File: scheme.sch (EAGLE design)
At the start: 34 parts, among them J1 22-05-7048-04, J2 22-05-7028-02

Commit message: Minor fix of routes
Signed-off-by: Nikita 'webconn' Maslov <wkernelteam@gmail.com>
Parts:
- R10, R9: device rcl:R-EU_R1206 -> resistor:R-EU_R0805
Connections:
- net PB5: now also R10.1; no longer R9.2
- net VCC: now also R9.2; no longer R10.1
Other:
- moved on the sheet: R10, R9
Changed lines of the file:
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@@
 <part name="P+17" library="supply1" deviceset="+12V" device=""/>
 <part name="P+19" library="supply1" deviceset="VCC" device=""/>
-<part name="R9" library="rcl" deviceset="R-EU_" device="R1206" value="0"/>
-<part name="R10" library="rcl" deviceset="R-EU_" device="R1206" value="0"/>
 <part name="P+18" library="supply1" deviceset="VCC" device=""/>
 <part name="J2" library="con-molex" deviceset="22-?-02" device="05-7028"/>
+<part name="R9" library="resistor" deviceset="R-EU_" device="R0805" value="0"/>
+<part name="R10" library="resistor" deviceset="R-EU_" device="R0805" value="0"/>
 </parts>
 <sheets>
@@
 <instance part="P+17" gate="1" x="68.58" y="45.72" rot="R180"/>
 <instance part="P+19" gate="VCC" x="83.82" y="71.12"/>
-<instance part="R9" gate="G$1" x="139.7" y="71.12"/>
-<instance part="R10" gate="G$1" x="124.46" y="71.12"/>
 <instance part="P+18" gate="VCC" x="116.84" y="76.2"/>
 <instance part="J2" gate="-1" x="63.5" y="55.88" rot="R180"/>
 <instance part="J2" gate="-2" x="63.5" y="58.42" rot="R180"/>
+<instance part="R9" gate="G$1" x="124.46" y="71.12" rot="R180"/>
+<instance part="R10" gate="G$1" x="139.7" y="71.12" rot="R180"/>
 </instances>
 <busses>
@@
 </segment>
 <segment>
-<pinref part="R10" gate="G$1" pin="1"/>
 <wire x1="119.38" y1="71.12" x2="116.84" y2="71.12" width="0.1524" layer="91"/>
 <wire x1="116.84" y1="71.12" x2="116.84" y2="73.66" width="0.1524" layer="91"/>
 <pinref part="P+18" gate="VCC" pin="VCC"/>
+<pinref part="R9" gate="G$1" pin="2"/>
 </segment>
 </net>
@@
 </segment>
 <segment>
-<pinref part="R9" gate="G$1" pin="2"/>
 <wire x1="144.78" y1="71.12" x2="154.94" y2="71.12" width="0.1524" layer="91"/>
 <label x="149.86" y="71.12" size="1.778" layer="95"/>
+<pinref part="R10" gate="G$1" pin="1"/>
 </segment>
 </net>
@@
 <wire x1="111.76" y1="66.04" x2="132.08" y2="66.04" width="0.1524" layer="91"/>
 <wire x1="132.08" y1="66.04" x2="132.08" y2="71.12" width="0.1524" layer="91"/>
-<pinref part="R9" gate="G$1" pin="1"/>
 <wire x1="132.08" y1="71.12" x2="134.62" y2="71.12" width="0.1524" layer="91"/>
-<pinref part="R10" gate="G$1" pin="2"/>
 <wire x1="129.54" y1="71.12" x2="132.08" y2="71.12" width="0.1524" layer="91"/>
 <junction x="132.08" y="71.12"/>
-</segment>
-</net>
+<pinref part="R9" gate="G$1" pin="1"/>
+<pinref part="R10" gate="G$1" pin="2"/>
+</segment>
+</net>

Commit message: Add BOOT button and fix isolation
Signed-off-by: Nikita 'webconn' Maslov <wkernelteam@gmail.com>
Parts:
- removed LED1: (no value), SparkFun-LED:LED5MM
- added R11, R12: 0, rcl:R-EU_R1206
- added S2: (no value), switch-omron:31-XX
- R4: value 300 -> 10K
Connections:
- net RXLED renamed LED
- removed net N$12: LED1.A, R4.1
- removed net TXLED: LED1.C, U$1.(XCK1/CTS)PD5
- new net HWB: R4.1, S2.S, U$1.(HWB)PE2
- net +5V: now also U$4.+VOUT; no longer U$3.+VOUT
- net GND: now also R11.1, R11.2, R12.1, R12.2, S2.P
- net RELAY: now also U$1.(XCK1/CTS)PD5; no longer U$1.(HWB)PE2
- net VCC: now also U$3.+VOUT; no longer U$4.+VOUT
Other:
- moved on the sheet: R4, U$3, U$4

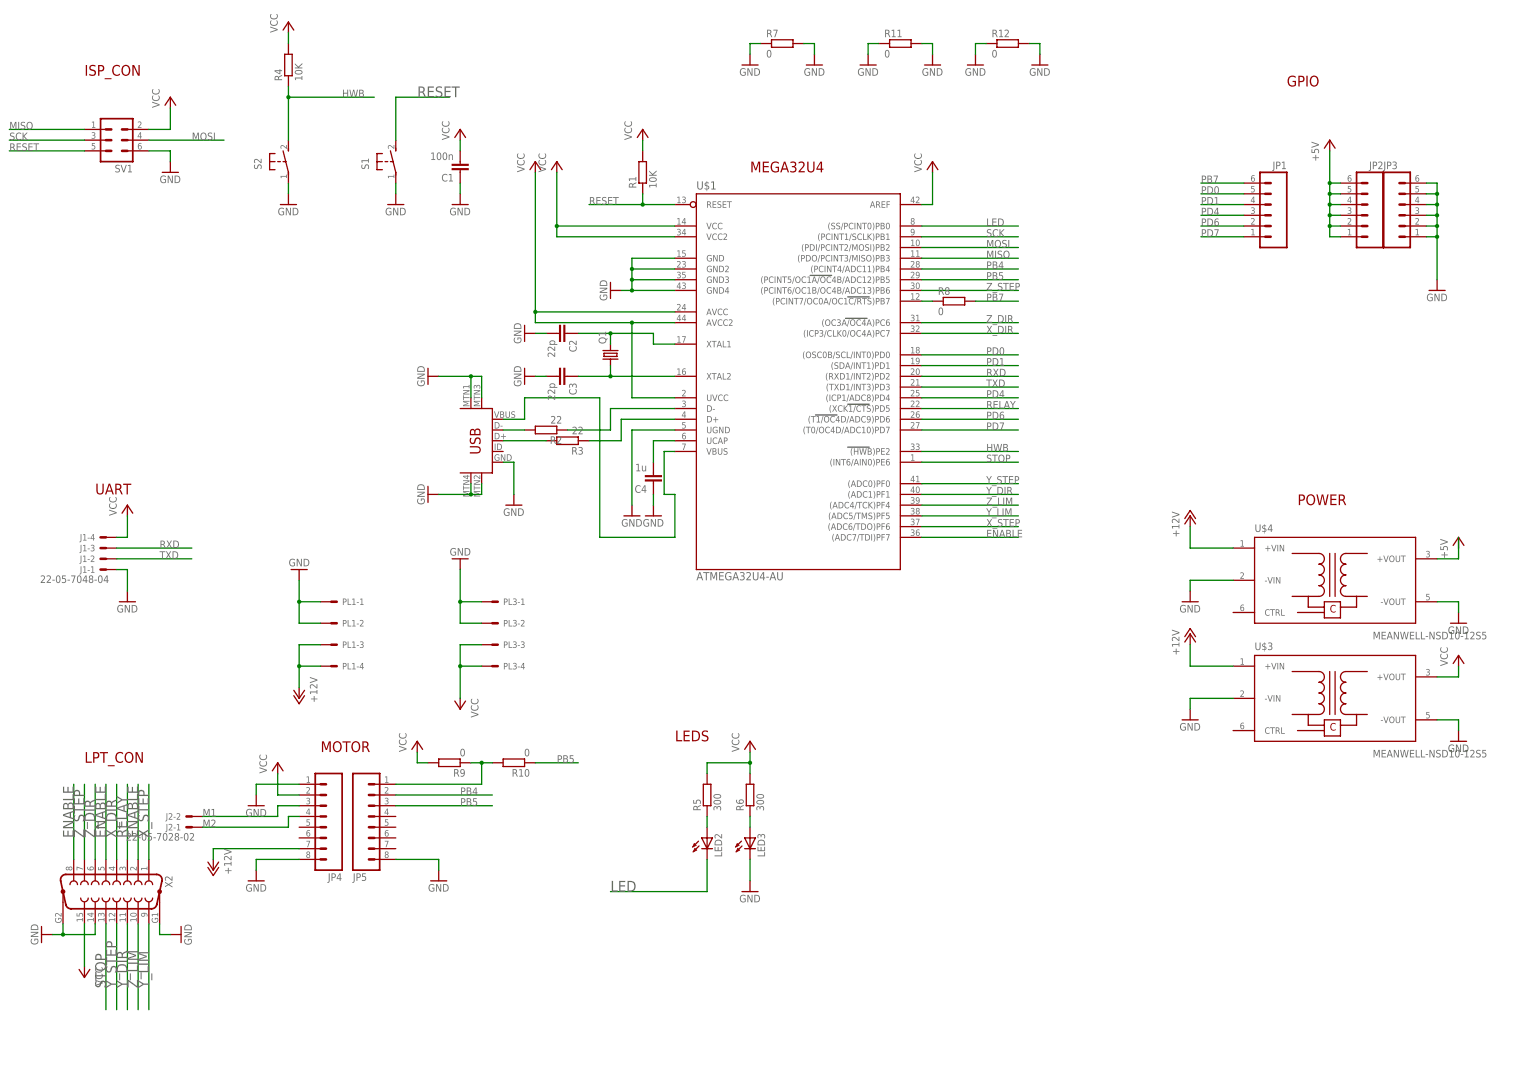
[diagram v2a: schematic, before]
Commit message: Add extra capacitors and rework silk
Signed-off-by: Nikita 'webconn' Maslov <wkernelteam@gmail.com>
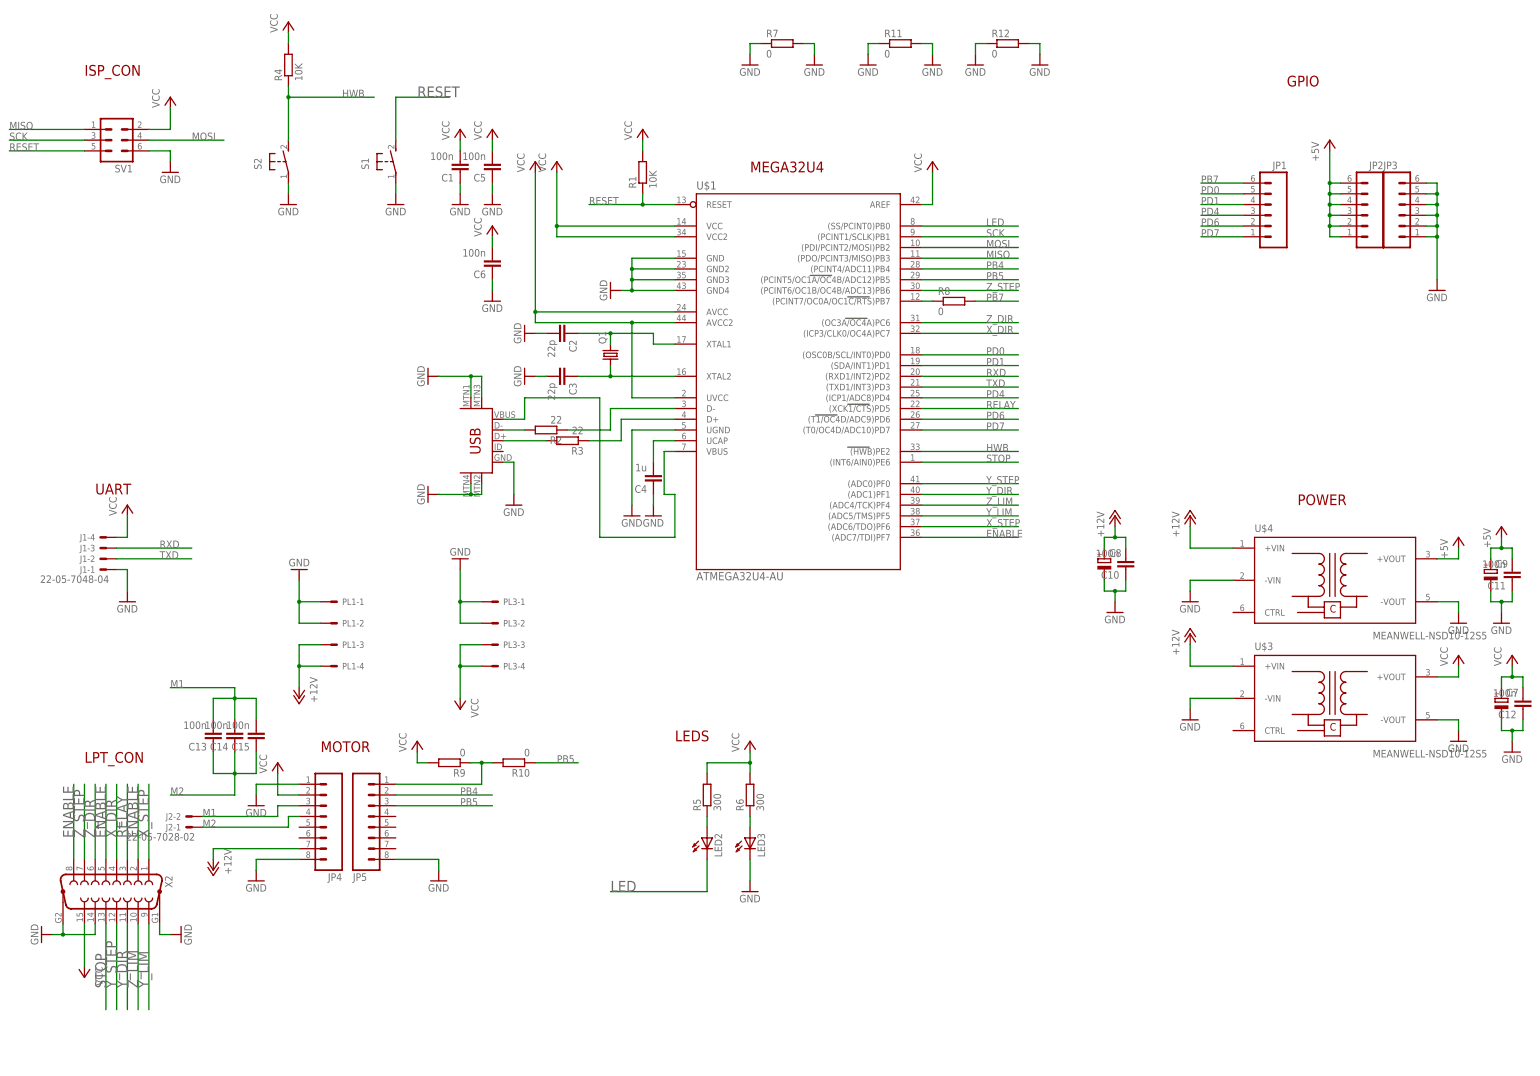
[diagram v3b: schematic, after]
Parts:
- added C10, C11, C12, C13, C14, C15, C5, C6: 100n, resistor:C-EUC0805
- added C7, C8, C9: (no value), rcl:CPOL-EUE2.5-6
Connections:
- net +12V: now also C10.2, C8.+
- net +5V: now also C11.2, C9.+
- net GND: now also C10.1, C11.1, C12.1, C5.1, C6.1, C7.-, C8.-, C9.-
- net M1: now also C13.2, C14.2, C15.2
- net M2: now also C13.1, C14.1, C15.1
- net VCC: now also C12.2, C5.2, C6.2, C7.+
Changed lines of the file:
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@@
 <part name="GND31" library="supply1" deviceset="GND" device=""/>
 <part name="GND32" library="supply1" deviceset="GND" device=""/>
+<part name="C5" library="resistor" deviceset="C-EU" device="C0805" value="100n"/>
+<part name="P+21" library="supply1" deviceset="VCC" device=""/>
+<part name="GND33" library="supply1" deviceset="GND" device=""/>
+<part name="C6" library="resistor" deviceset="C-EU" device="C0805" value="100n"/>
+<part name="P+22" library="supply1" deviceset="VCC" device=""/>
+<part name="GND34" library="supply1" deviceset="GND" device=""/>
+<part name="C8" library="rcl" deviceset="CPOL-EU" device="E2.5-6"/>
+<part name="C9" library="rcl" deviceset="CPOL-EU" device="E2.5-6"/>
+<part name="P+23" library="supply1" deviceset="+12V" device=""/>
+<part name="GND35" library="supply1" deviceset="GND" device=""/>
+<part name="P+24" library="supply1" deviceset="+5V" device=""/>
+<part name="GND36" library="supply1" deviceset="GND" device=""/>
+<part name="C7" library="rcl" deviceset="CPOL-EU" device="E2.5-6"/>
+<part name="P+25" library="supply1" deviceset="VCC" device=""/>
+<part name="GND37" library="supply1" deviceset="GND" device=""/>
+<part name="C10" library="resistor" deviceset="C-EU" device="C0805" value="100n"/>
+<part name="C11" library="resistor" deviceset="C-EU" device="C0805" value="100n"/>
+<part name="C12" library="resistor" deviceset="C-EU" device="C0805" value="100n"/>
+<part name="C13" library="resistor" deviceset="C-EU" device="C0805" value="100n"/>
+<part name="C14" library="resistor" deviceset="C-EU" device="C0805" value="100n"/>
+<part name="C15" library="resistor" deviceset="C-EU" device="C0805" value="100n"/>
 </parts>
 <sheets>
@@
 <instance part="GND31" gate="1" x="248.92" y="236.22"/>
 <instance part="GND32" gate="1" x="264.16" y="236.22"/>
+<instance part="C5" gate="G$1" x="134.62" y="210.82" rot="R180"/>
+<instance part="P+21" gate="VCC" x="134.62" y="220.98"/>
+<instance part="GND33" gate="1" x="134.62" y="203.2"/>
+<instance part="C6" gate="G$1" x="134.62" y="187.96" rot="R180"/>
+<instance part="P+22" gate="VCC" x="134.62" y="198.12"/>
+<instance part="GND34" gate="1" x="134.62" y="180.34"/>
+<instance part="C8" gate="G$1" x="279.4" y="119.38"/>
+<instance part="C9" gate="G$1" x="370.84" y="116.84"/>
+<instance part="P+23" gate="1" x="281.94" y="129.54"/>
+<instance part="GND35" gate="1" x="281.94" y="106.68"/>
+<instance part="P+24" gate="1" x="373.38" y="127"/>
+<instance part="GND36" gate="1" x="373.38" y="104.14"/>
+<instance part="C7" gate="G$1" x="373.38" y="86.36"/>
+<instance part="P+25" gate="VCC" x="375.92" y="96.52"/>
+<instance part="GND37" gate="1" x="375.92" y="73.66"/>
+<instance part="C10" gate="G$1" x="284.48" y="116.84" rot="R180"/>
+<instance part="C11" gate="G$1" x="375.92" y="114.3" rot="R180"/>
+<instance part="C12" gate="G$1" x="378.46" y="83.82" rot="R180"/>
+<instance part="C13" gate="G$1" x="68.58" y="76.2" rot="R180"/>
+<instance part="C14" gate="G$1" x="73.66" y="76.2" rot="R180"/>
+<instance part="C15" gate="G$1" x="78.74" y="76.2" rot="R180"/>
 </instances>
 <busses>
@@
 <wire x1="264.16" y1="241.3" x2="264.16" y2="238.76" width="0.1524" layer="91"/>
 </segment>
+<segment>
+<pinref part="C5" gate="G$1" pin="1"/>
+<pinref part="GND33" gate="1" pin="GND"/>
+<wire x1="134.62" y1="208.28" x2="134.62" y2="205.74" width="0.1524" layer="91"/>
+</segment>
+<segment>
+<pinref part="C6" gate="G$1" pin="1"/>
+<pinref part="GND34" gate="1" pin="GND"/>
+<wire x1="134.62" y1="185.42" x2="134.62" y2="182.88" width="0.1524" layer="91"/>
+</segment>
+<segment>
+<pinref part="C8" gate="G$1" pin="-"/>
+<wire x1="279.4" y1="114.3" x2="279.4" y2="111.76" width="0.1524" layer="91"/>
+<wire x1="279.4" y1="111.76" x2="281.94" y2="111.76" width="0.1524" layer="91"/>
+<pinref part="GND35" gate="1" pin="GND"/>
+<wire x1="281.94" y1="111.76" x2="281.94" y2="109.22" width="0.1524" layer="91"/>
+<pinref part="C10" gate="G$1" pin="1"/>
+<wire x1="281.94" y1="111.76" x2="284.48" y2="111.76" width="0.1524" layer="91"/>
+<wire x1="284.48" y1="111.76" x2="284.48" y2="114.3" width="0.1524" layer="91"/>
+<junction x="281.94" y="111.76"/>
+</segment>
+<segment>
+<pinref part="C9" gate="G$1" pin="-"/>
+<wire x1="370.84" y1="111.76" x2="370.84" y2="109.22" width="0.1524" layer="91"/>
+<wire x1="370.84" y1="109.22" x2="373.38" y2="109.22" width="0.1524" layer="91"/>
+<pinref part="GND36" gate="1" pin="GND"/>
+<wire x1="373.38" y1="109.22" x2="373.38" y2="106.68" width="0.1524" layer="91"/>
+<pinref part="C11" gate="G$1" pin="1"/>
+<wire x1="373.38" y1="109.22" x2="375.92" y2="109.22" width="0.1524" layer="91"/>
+<wire x1="375.92" y1="109.22" x2="375.92" y2="111.76" width="0.1524" layer="91"/>
+<junction x="373.38" y="109.22"/>
+</segment>
+<segment>
+<pinref part="C7" gate="G$1" pin="-"/>
+<wire x1="373.38" y1="81.28" x2="373.38" y2="78.74" width="0.1524" layer="91"/>
+<pinref part="C12" gate="G$1" pin="1"/>
+<wire x1="373.38" y1="78.74" x2="375.92" y2="78.74" width="0.1524" layer="91"/>
+<wire x1="375.92" y1="78.74" x2="378.46" y2="78.74" width="0.1524" layer="91"/>
+<wire x1="378.46" y1="78.74" x2="378.46" y2="81.28" width="0.1524" layer="91"/>
+<pinref part="GND37" gate="1" pin="GND"/>
+<wire x1="375.92" y1="78.74" x2="375.92" y2="76.2" width="0.1524" layer="91"/>
+<junction x="375.92" y="78.74"/>
+</segment>
 </net>
 <net name="RESET" class="0">
@@
 <wire x1="86.36" y1="243.84" x2="86.36" y2="241.3" width="0.1524" layer="91"/>
 </segment>
+<segment>
+<pinref part="P+21" gate="VCC" pin="VCC"/>
+<pinref part="C5" gate="G$1" pin="2"/>
+<wire x1="134.62" y1="218.44" x2="134.62" y2="215.9" width="0.1524" layer="91"/>
+</segment>
+<segment>
+<pinref part="P+22" gate="VCC" pin="VCC"/>
+<pinref part="C6" gate="G$1" pin="2"/>
+<wire x1="134.62" y1="195.58" x2="134.62" y2="193.04" width="0.1524" layer="91"/>
+</segment>
+<segment>
+<pinref part="C7" gate="G$1" pin="+"/>
+<wire x1="373.38" y1="88.9" x2="373.38" y2="91.44" width="0.1524" layer="91"/>
+<pinref part="C12" gate="G$1" pin="2"/>
+<wire x1="373.38" y1="91.44" x2="375.92" y2="91.44" width="0.1524" layer="91"/>
+<wire x1="375.92" y1="91.44" x2="378.46" y2="91.44" width="0.1524" layer="91"/>
+<wire x1="378.46" y1="91.44" x2="378.46" y2="88.9" width="0.1524" layer="91"/>
+<pinref part="P+25" gate="VCC" pin="VCC"/>
+<wire x1="375.92" y1="91.44" x2="375.92" y2="93.98" width="0.1524" layer="91"/>
+<junction x="375.92" y="91.44"/>
+</segment>
 </net>
 <net name="N$4" class="0">
@@
 <wire x1="68.58" y1="50.8" x2="68.58" y2="48.26" width="0.1524" layer="91"/>
 <pinref part="P+17" gate="1" pin="+12V"/>
+</segment>
+<segment>
+<pinref part="C8" gate="G$1" pin="+"/>
+<wire x1="279.4" y1="121.92" x2="279.4" y2="124.46" width="0.1524" layer="91"/>
+<wire x1="279.4" y1="124.46" x2="281.94" y2="124.46" width="0.1524" layer="91"/>
+<pinref part="P+23" gate="1" pin="+12V"/>
+<wire x1="281.94" y1="127" x2="281.94" y2="124.46" width="0.1524" layer="91"/>
+<pinref part="C10" gate="G$1" pin="2"/>
+<wire x1="281.94" y1="124.46" x2="284.48" y2="124.46" width="0.1524" layer="91"/>
+<wire x1="284.48" y1="124.46" x2="284.48" y2="121.92" width="0.1524" layer="91"/>
+<junction x="281.94" y="124.46"/>
 </segment>
 </net>
@@
 <wire x1="358.14" y1="119.38" x2="363.22" y2="119.38" width="0.1524" layer="91"/>
 <wire x1="363.22" y1="119.38" x2="363.22" y2="121.92" width="0.1524" layer="91"/>
-<wire x1="363.22" y1="121.92" x2="363.22" y2="124.46" width="0.1524" layer="91"/>
 <pinref part="U$4" gate="G$1" pin="+VOUT"/>
+</segment>
+<segment>
+<pinref part="C9" gate="G$1" pin="+"/>
+<wire x1="370.84" y1="119.38" x2="370.84" y2="121.92" width="0.1524" layer="91"/>
+<wire x1="370.84" y1="121.92" x2="373.38" y2="121.92" width="0.1524" layer="91"/>
+<pinref part="P+24" gate="1" pin="+5V"/>
+<wire x1="373.38" y1="121.92" x2="373.38" y2="124.46" width="0.1524" layer="91"/>
+<pinref part="C11" gate="G$1" pin="2"/>
+<wire x1="373.38" y1="121.92" x2="375.92" y2="121.92" width="0.1524" layer="91"/>
+<wire x1="375.92" y1="121.92" x2="375.92" y2="119.38" width="0.1524" layer="91"/>
+<junction x="373.38" y="121.92"/>
 </segment>
 </net>
@@
 <pinref part="J2" gate="-2" pin="S"/>
 </segment>
+<segment>
+<pinref part="C13" gate="G$1" pin="2"/>
+<wire x1="68.58" y1="81.28" x2="68.58" y2="86.36" width="0.1524" layer="91"/>
+<pinref part="C14" gate="G$1" pin="2"/>
+<wire x1="73.66" y1="81.28" x2="73.66" y2="86.36" width="0.1524" layer="91"/>
+<wire x1="68.58" y1="86.36" x2="73.66" y2="86.36" width="0.1524" layer="91"/>
+<pinref part="C15" gate="G$1" pin="2"/>
+<wire x1="78.74" y1="81.28" x2="78.74" y2="86.36" width="0.1524" layer="91"/>
+<wire x1="73.66" y1="86.36" x2="78.74" y2="86.36" width="0.1524" layer="91"/>
+<junction x="73.66" y="86.36"/>
+<wire x1="73.66" y1="86.36" x2="73.66" y2="88.9" width="0.1524" layer="91"/>
+<wire x1="73.66" y1="88.9" x2="58.42" y2="88.9" width="0.1524" layer="91"/>
+<label x="58.42" y="88.9" size="1.778" layer="95"/>
+</segment>
 </net>
 <net name="M2" class="0">
@@
 <pinref part="J2" gate="-1" pin="S"/>
 </segment>
-</net>
+<segment>
+<pinref part="C13" gate="G$1" pin="1"/>
+<wire x1="68.58" y1="73.66" x2="68.58" y2="68.58" width="0.1524" layer="91"/>
+<pinref part="C14" gate="G$1" pin="1"/>
+<wire x1="73.66" y1="73.66" x2="73.66" y2="68.58" width="0.1524" layer="91"/>
+<pinref part="C15" gate="G$1" pin="1"/>
+<wire x1="78.74" y1="73.66" x2="78.74" y2="68.58" width="0.1524" layer="91"/>
+<wire x1="73.66" y1="68.58" x2="78.74" y2="68.58" width="0.1524" layer="91"/>
+<wire x1="68.58" y1="68.58" x2="73.66" y2="68.58" width="0.1524" layer="91"/>
+<junction x="73.66" y="68.58"/>
+<wire x1="73.66" y1="68.58" x2="73.66" y2="63.5" width="0.1524" layer="91"/>
+<wire x1="73.66" y1="63.5" x2="58.42" y2="63.5" width="0.1524" layer="91"/>
+<label x="58.42" y="63.5" size="1.778" layer="95"/>
+</segment>
+</net>

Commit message: Add USB power jumper
Signed-off-by: Nikita 'webconn' Maslov <wkernelteam@gmail.com>
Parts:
- added JP6: M02PTH, SparkFun-Connectors:M02PTH
- added R13: 0, rcl:R-EU_R1206
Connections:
- new net N$12: JP6.1, R13.1
- net N$11: now also R13.2
- net VCC: now also JP6.2
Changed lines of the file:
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@@
 <part name="C14" library="resistor" deviceset="C-EU" device="C0805" value="100n"/>
 <part name="C15" library="resistor" deviceset="C-EU" device="C0805" value="100n"/>
+<part name="JP6" library="SparkFun-Connectors" deviceset="M02" device="PTH"/>
+<part name="P+26" library="supply1" deviceset="VCC" device=""/>
+<part name="R13" library="rcl" deviceset="R-EU_" device="R1206" value="0"/>
 </parts>
 <sheets>
@@
 <instance part="C14" gate="G$1" x="73.66" y="76.2" rot="R180"/>
 <instance part="C15" gate="G$1" x="78.74" y="76.2" rot="R180"/>
+<instance part="JP6" gate="G$1" x="175.26" y="116.84" rot="R180"/>
+<instance part="P+26" gate="VCC" x="157.48" y="114.3" rot="R90"/>
+<instance part="R13" gate="G$1" x="154.94" y="124.46" rot="R90"/>
 </instances>
 <busses>
@@
 <junction x="375.92" y="91.44"/>
 </segment>
+<segment>
+<pinref part="P+26" gate="VCC" pin="VCC"/>
+<pinref part="JP6" gate="G$1" pin="2"/>
+<wire x1="160.02" y1="114.3" x2="167.64" y2="114.3" width="0.1524" layer="91"/>
+</segment>
 </net>
 <net name="N$4" class="0">
@@
 <wire x1="177.8" y1="134.62" x2="177.8" y2="124.46" width="0.1524" layer="91"/>
 <wire x1="177.8" y1="124.46" x2="160.02" y2="124.46" width="0.1524" layer="91"/>
-<wire x1="160.02" y1="124.46" x2="160.02" y2="157.48" width="0.1524" layer="91"/>
+<wire x1="160.02" y1="124.46" x2="160.02" y2="132.08" width="0.1524" layer="91"/>
 <pinref part="U$2" gate="G$1" pin="VBUS"/>
+<wire x1="160.02" y1="132.08" x2="160.02" y2="157.48" width="0.1524" layer="91"/>
 <wire x1="142.24" y1="157.48" x2="142.24" y2="152.4" width="0.1524" layer="91"/>
 <wire x1="142.24" y1="152.4" x2="137.16" y2="152.4" width="0.1524" layer="91"/>
 <wire x1="160.02" y1="157.48" x2="142.24" y2="157.48" width="0.1524" layer="91"/>
+<pinref part="R13" gate="G$1" pin="2"/>
+<wire x1="160.02" y1="132.08" x2="154.94" y2="132.08" width="0.1524" layer="91"/>
+<wire x1="154.94" y1="132.08" x2="154.94" y2="129.54" width="0.1524" layer="91"/>
+<junction x="160.02" y="132.08"/>
 </segment>
 </net>
@@
 </segment>
 </net>
+<net name="N$12" class="0">
+<segment>
+<pinref part="JP6" gate="G$1" pin="1"/>
+<pinref part="R13" gate="G$1" pin="1"/>
+<wire x1="154.94" y1="119.38" x2="154.94" y2="116.84" width="0.1524" layer="91"/>
+<wire x1="154.94" y1="116.84" x2="167.64" y2="116.84" width="0.1524" layer="91"/>
+</segment>
+</net>
